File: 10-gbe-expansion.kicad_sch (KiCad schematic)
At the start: 0 parts

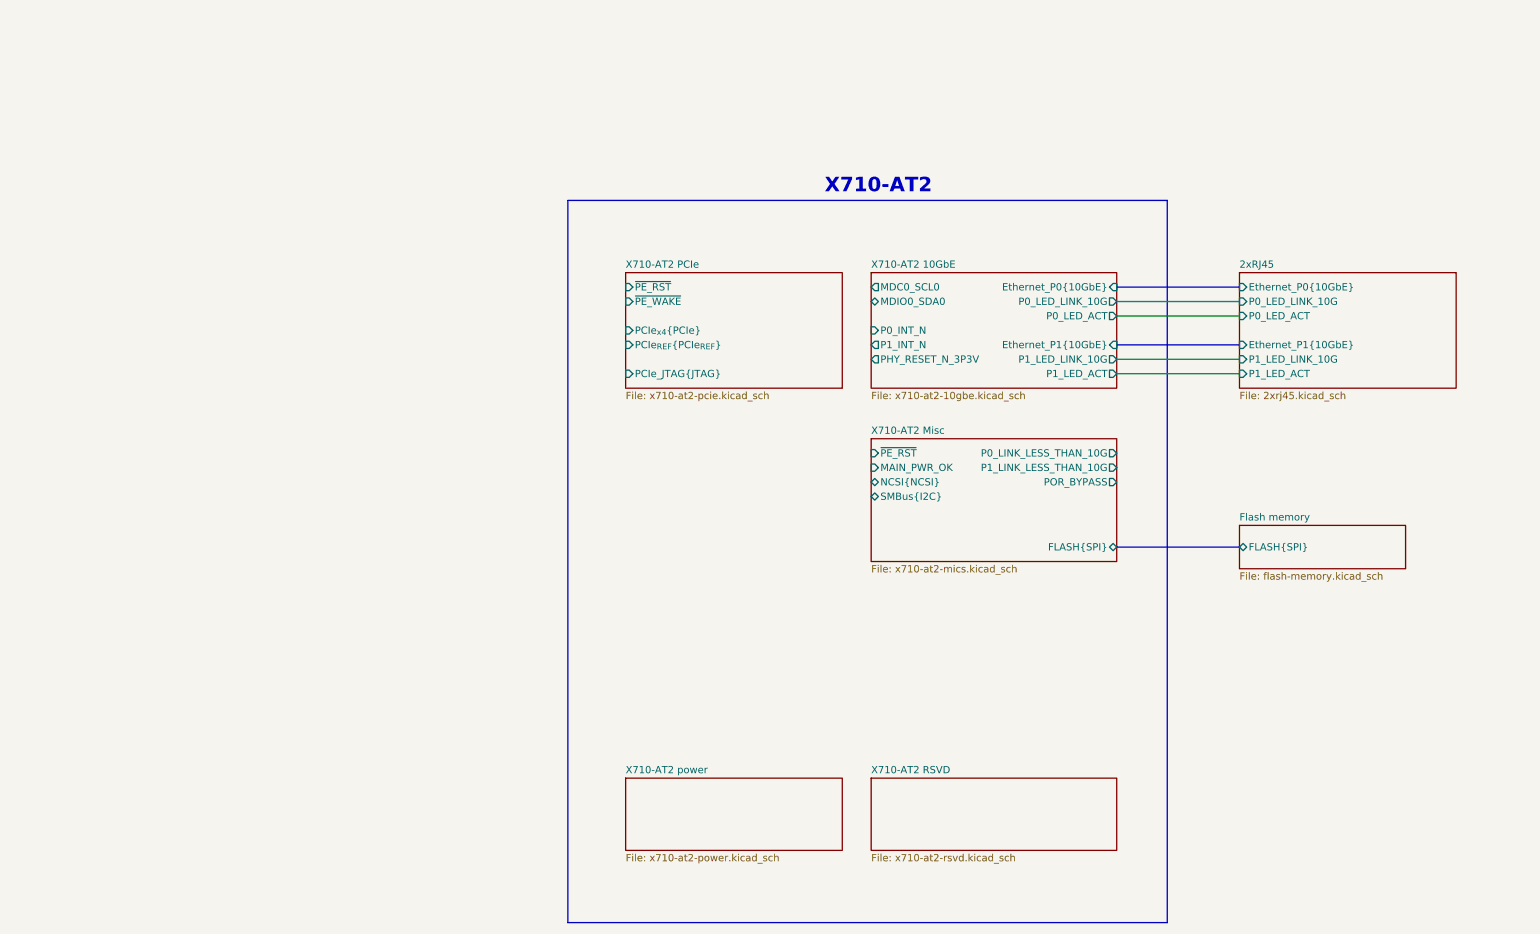
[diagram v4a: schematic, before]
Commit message: [#80813] Add power supply sheet, reorder schematic hierarchy
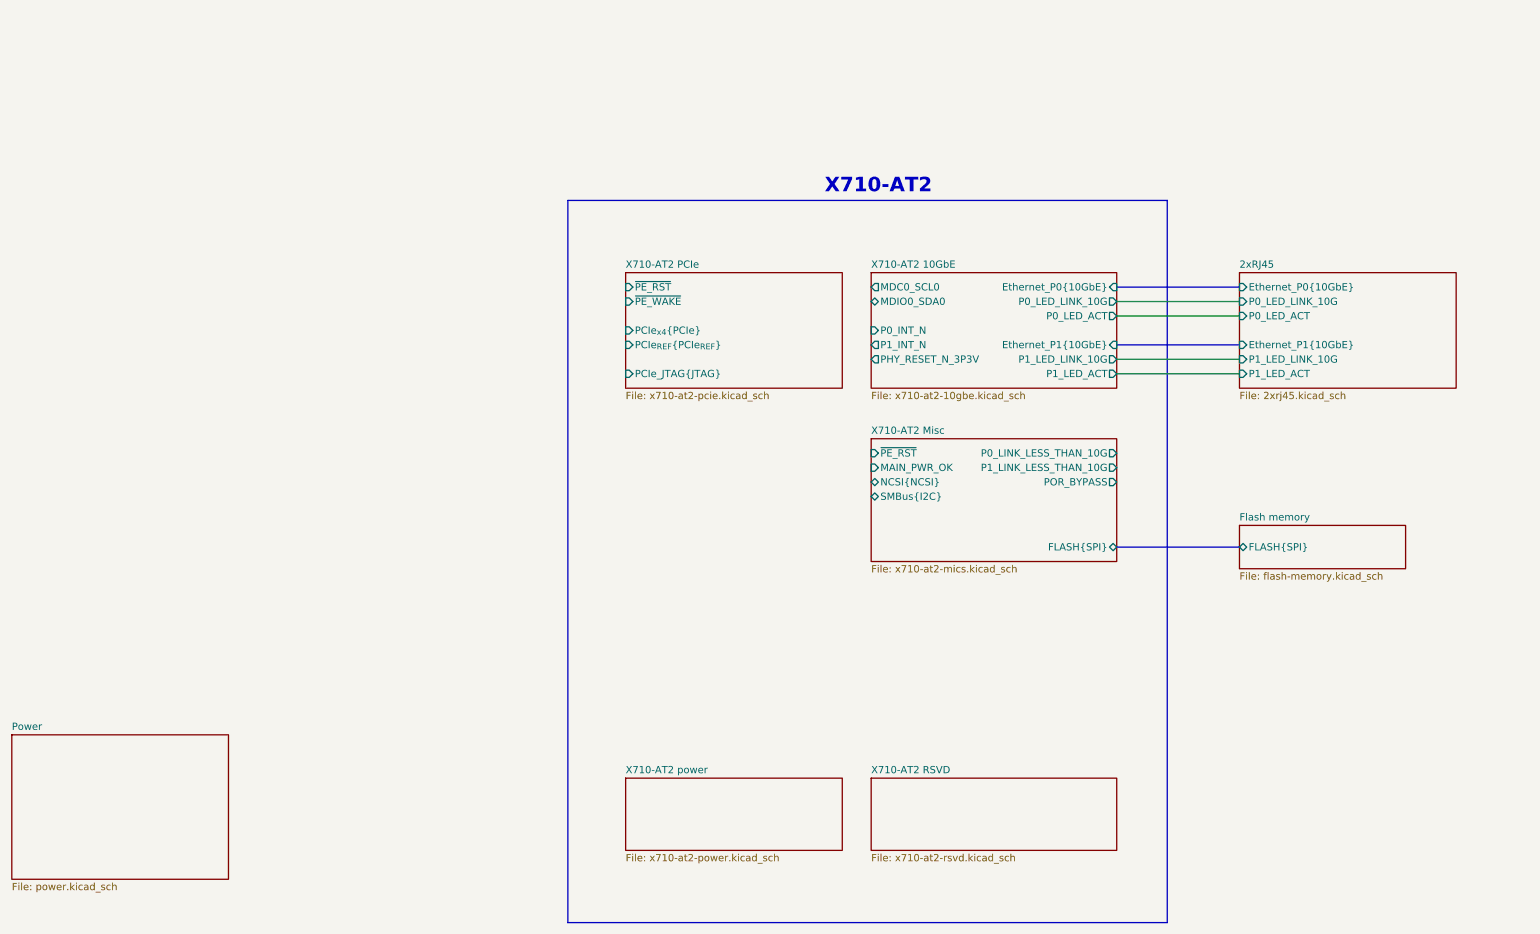
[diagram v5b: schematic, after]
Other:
- added sheet Power (power.kicad_sch)
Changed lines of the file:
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@@
 			(project "10-gbe-expansion"
 				(path "/04bda987-e5eb-48b4-9e90-d8211dc11b39"
-					(page "3")
+					(page "6")
+				)
+			)
+		)
+	)
+	(sheet
+		(at 76.2 177.8)
+		(size 38.1 25.4)
+		(exclude_from_sim no)
+		(in_bom yes)
+		(on_board yes)
+		(dnp no)
+		(fields_autoplaced yes)
+		(stroke
+			(width 0.1524)
+			(type solid)
+		)
+		(fill
+			(color 255 255 194 1.0000)
+		)
+		(property "Sheetname" "Power"
+			(at 76.2 177.0884 0)
+			(effects
+				(font
+					(size 1.27 1.27)
+				)
+				(justify left bottom)
+			)
+		)
+		(property "Sheetfile" "power.kicad_sch"
+			(at 76.2 203.7846 0)
+			(effects
+				(font
+					(size 1.27 1.27)
+				)
+				(justify left top)
+			)
+		)
+		(instances
+			(project "10-gbe-expansion"
+				(path "/04bda987-e5eb-48b4-9e90-d8211dc11b39"
+					(page "2")
 				)
 			)
@@
 			(project "10-gbe-expansion"
 				(path "/04bda987-e5eb-48b4-9e90-d8211dc11b39"
-					(page "4")
+					(page "7")
 				)
 			)
@@
 			(project "10-gbe-expansion"
 				(path "/04bda987-e5eb-48b4-9e90-d8211dc11b39"
-					(page "5")
+					(page "9")
 				)
 			)
@@
 			(project "10-gbe-expansion"
 				(path "/04bda987-e5eb-48b4-9e90-d8211dc11b39"
-					(page "4")
+					(page "5")
 				)
 			)
@@
 		(fields_autoplaced yes)
 		(stroke
-			(width 0.1524)
+			(width 0.1016)
 			(type solid)
 		)
@@
 			(project "10-gbe-expansion"
 				(path "/04bda987-e5eb-48b4-9e90-d8211dc11b39"
-					(page "7")
+					(page "4")
 				)
 			)
@@
 			(project "10-gbe-expansion"
 				(path "/04bda987-e5eb-48b4-9e90-d8211dc11b39"
-					(page "8")
+					(page "3")
 				)
 			)
@@
 			(project "10-gbe-expansion"
 				(path "/04bda987-e5eb-48b4-9e90-d8211dc11b39"
-					(page "6")
-				)
-			)
+					(page "8")
+				)
+			)

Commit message: [#80813] Add misc, improve schematic readability
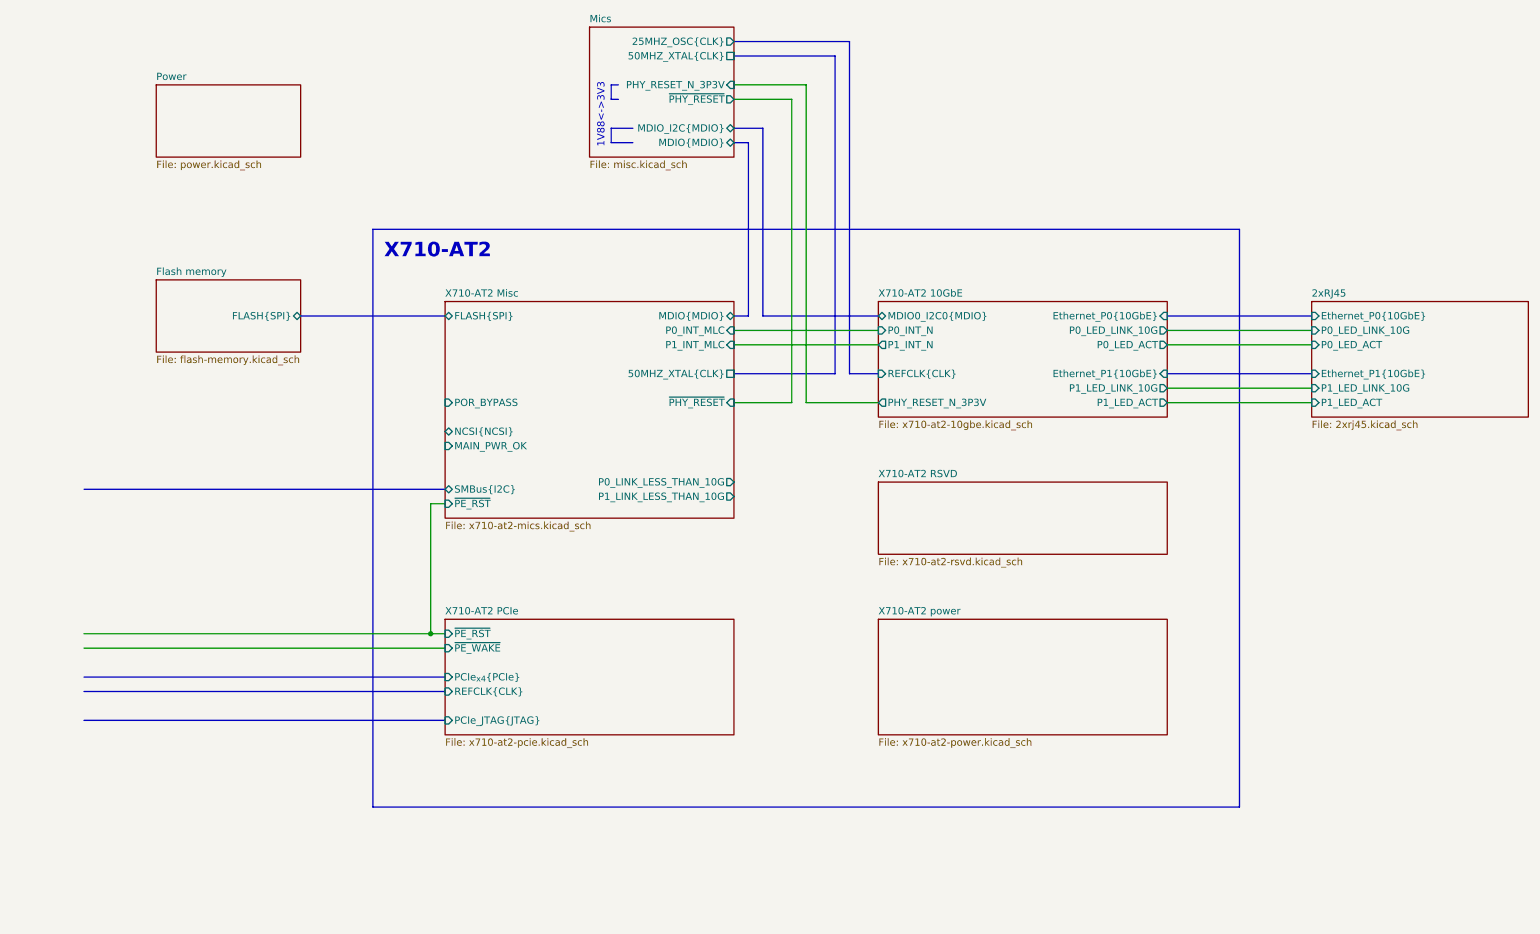
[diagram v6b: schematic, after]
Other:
- added sheet Mics (misc.kicad_sch)
- sheet X710-AT2 10GbE ports: added MDIO0_I2C0{MDIO}, REFCLK{CLK}; removed MDC0_SCL0, MDIO0_SDA0
- sheet X710-AT2 Misc ports: added 50MHZ_XTAL{CLK}, MDIO{MDIO}, P0_INT_MLC, P1_INT_MLC, ~{PHY_RESET}; removed none
- sheet X710-AT2 PCIe ports: added REFCLK{CLK}; removed PCIe_{REF}{PCIe_{REF}}
- note added: "1V88<->3V3"

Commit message: [#80813] Change RJ45 connectors, reannotate schematics
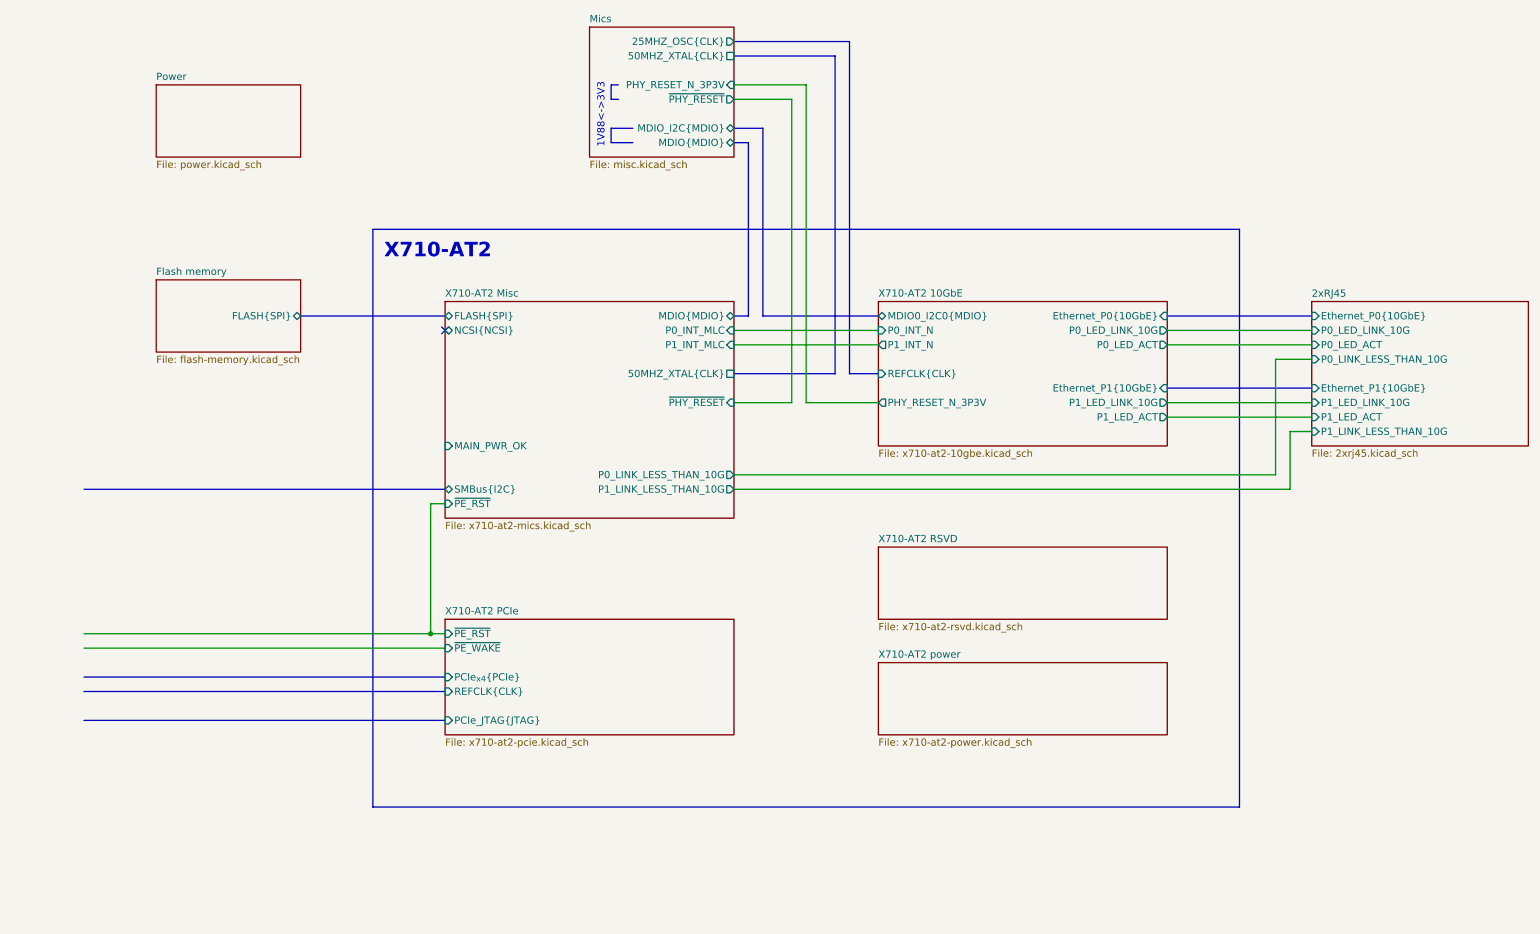
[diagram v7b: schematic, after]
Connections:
- no-connect marks 0 -> 1
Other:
- sheet 2xRJ45 ports: added P0_LINK_LESS_THAN_10G, P1_LINK_LESS_THAN_10G; removed none
- sheet X710-AT2 Misc ports: added none; removed POR_BYPASS

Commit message: [#80813] Improve schematic readability, add debug connectors and missing resistors
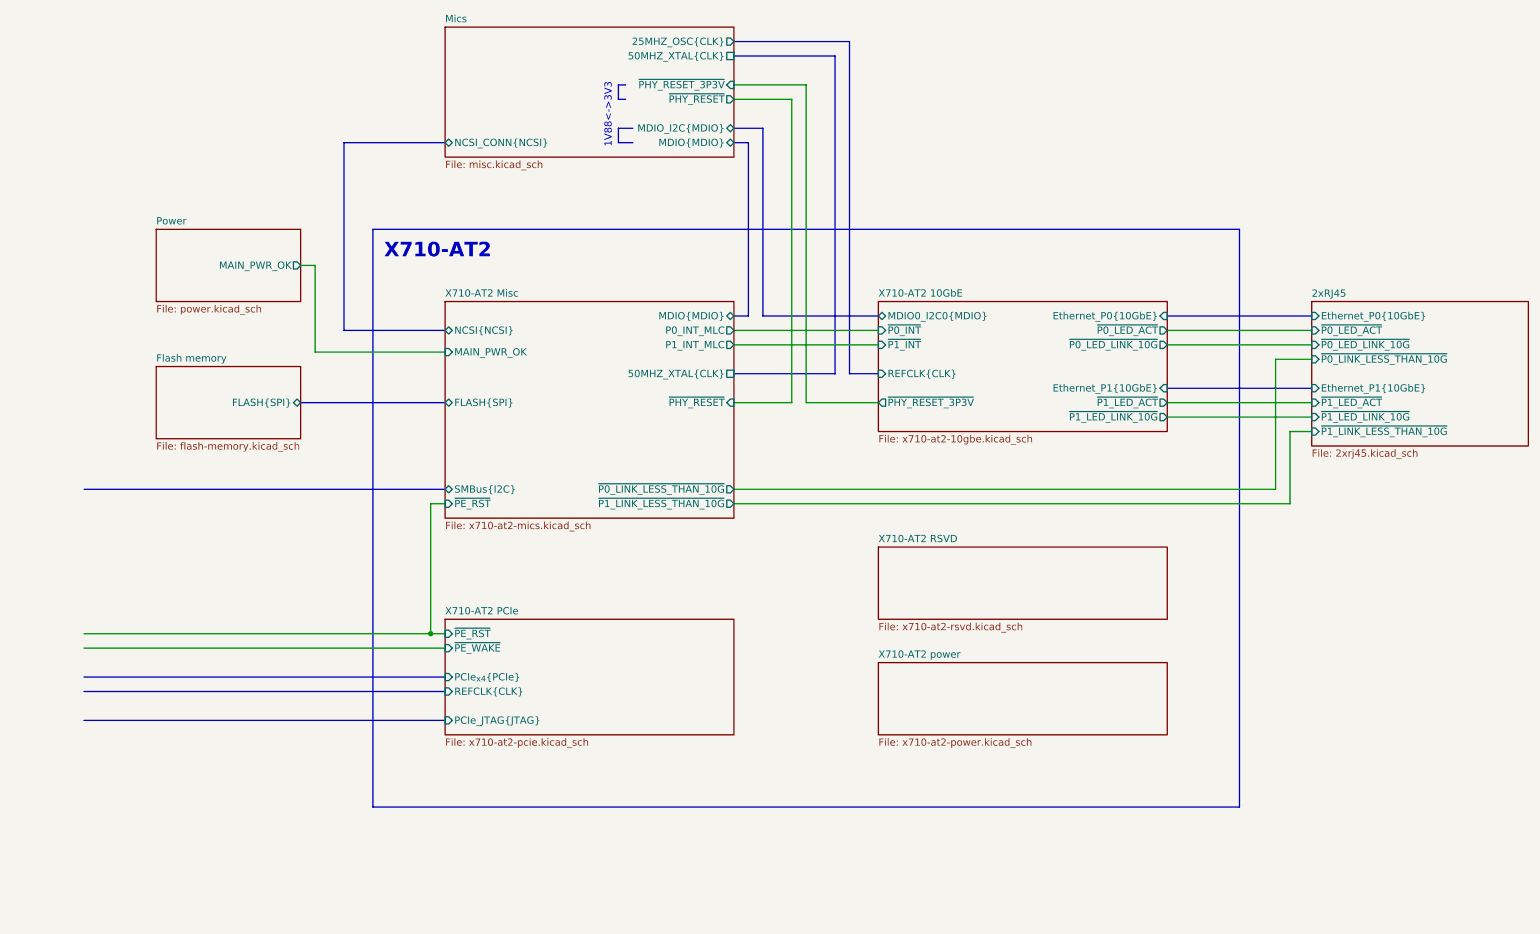
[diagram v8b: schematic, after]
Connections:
- no-connect marks 1 -> 0
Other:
- sheet 2xRJ45 ports: added ~{P0_LED_ACT}, ~{P0_LED_LINK_10G}, ~{P0_LINK_LESS_THAN_10G}, ~{P1_LED_ACT}, ~{P1_LED_LINK_10G}, ~{P1_LINK_LESS_THAN_10G}; removed P0_LED_ACT, P0_LED_LINK_10G, P0_LINK_LESS_THAN_10G, P1_LED_ACT, P1_LED_LINK_10G, P1_LINK_LESS_THAN_10G
- sheet Mics ports: added NCSI_CONN{NCSI}, ~{PHY_RESET_3P3V}; removed PHY_RESET_N_3P3V
- sheet Power ports: added MAIN_PWR_OK; removed none
- sheet X710-AT2 10GbE ports: added ~{P0_INT}, ~{P0_LED_ACT}, ~{P0_LED_LINK_10G}, ~{P1_INT}, ~{P1_LED_ACT}, ~{P1_LED_LINK_10G}, ~{PHY_RESET_3P3V}; removed P0_INT_N, P0_LED_ACT, P0_LED_LINK_10G, P1_INT_N, P1_LED_ACT, P1_LED_LINK_10G, PHY_RESET_N_3P3V
- sheet X710-AT2 Misc ports: added ~{P0_LINK_LESS_THAN_10G}, ~{P1_LINK_LESS_THAN_10G}; removed P0_LINK_LESS_THAN_10G, P1_LINK_LESS_THAN_10G
